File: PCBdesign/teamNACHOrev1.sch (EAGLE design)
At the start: 3 parts

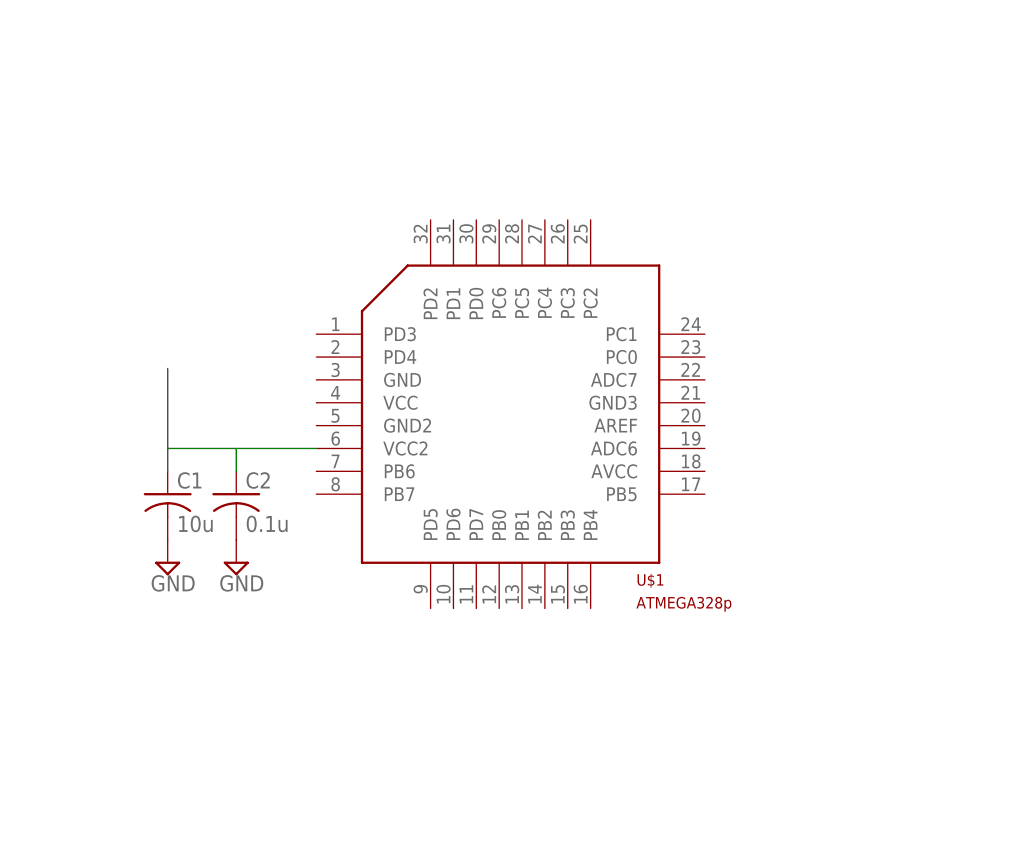
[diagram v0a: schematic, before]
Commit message: ATmega
Believe the initial set up of atmega328p has been done.
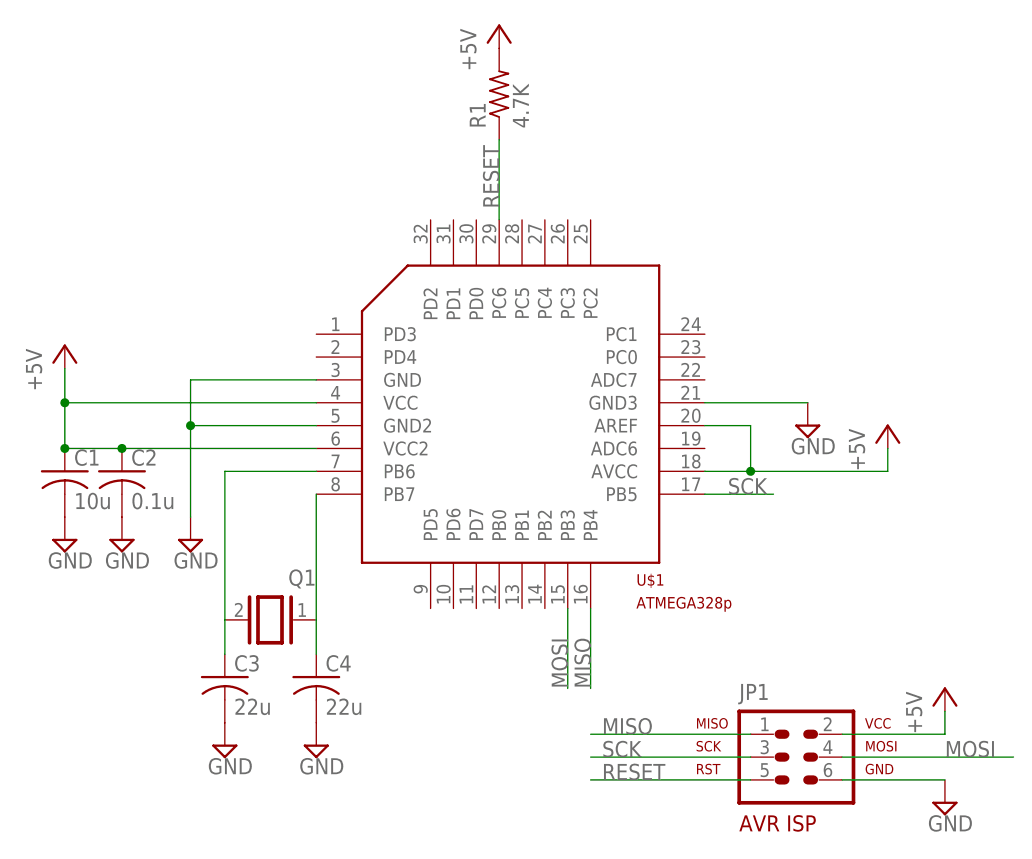
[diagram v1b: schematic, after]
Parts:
- added C3, C4: 22u, rcl:C-USC0805
- added JP1: AVR-ISP-6VERT, avr-7:AVR-ISP-6VERT
- added Q1: (no value), special:XTAL/S
- added R1: 4.7K, rcl:R-US_R0805
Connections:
- removed net N$1: C1.1, C2.1, U$1.VCC2
- new net +5V: C1.1, C2.1, JP1.2, R1.2, U$1.AREF, U$1.AVCC, U$1.VCC, U$1.VCC2
- new net MISO: JP1.1, U$1.PB4
- new net MOSI: JP1.4, U$1.PB3
- new net N$2: C3.1, Q1.2, U$1.PB6
- new net N$3: C4.1, Q1.1, U$1.PB7
- new net RESET: JP1.5, R1.1, U$1.PC6
- new net SCK: JP1.3, U$1.PB5
- net GND: now also C3.2, C4.2, JP1.6, U$1.GND, U$1.GND2, U$1.GND3
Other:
- moved on the sheet: C1, C2
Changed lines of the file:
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@@
 <layer number="48" name="Document" color="7" fill="1" visible="no" active="no"/>
 <layer number="49" name="Reference" color="7" fill="1" visible="no" active="no"/>
+<layer number="50" name="dxf" color="7" fill="1" visible="no" active="no"/>
 <layer number="51" name="tDocu" color="7" fill="1" visible="no" active="no"/>
 <layer number="52" name="bDocu" color="7" fill="1" visible="no" active="no"/>
@@
 <layer number="97" name="Info" color="7" fill="1" visible="yes" active="yes"/>
 <layer number="98" name="Guide" color="6" fill="1" visible="yes" active="yes"/>
+<layer number="200" name="200bmp" color="1" fill="10" visible="no" active="no"/>
 </layers>
 <schematic xreflabel="%F%N/%S.%C%R" xrefpart="/%S.%C%R">
@@
 <part name="SUPPLY1" library="supply2" deviceset="GND" device=""/>
 <part name="SUPPLY2" library="supply2" deviceset="GND" device=""/>
+<part name="Q1" library="special" deviceset="XTAL/S" device=""/>
+<part name="C3" library="rcl" deviceset="C-US" device="C0805" value="22u"/>
+<part name="C4" library="rcl" deviceset="C-US" device="C0805" value="22u"/>
+<part name="SUPPLY3" library="supply2" deviceset="GND" device=""/>
+<part name="SUPPLY4" library="supply2" deviceset="GND" device=""/>
+<part name="SUPPLY5" library="supply2" deviceset="GND" device=""/>
+<part name="P+1" library="supply1" deviceset="+5V" device=""/>
+<part name="SUPPLY6" library="supply2" deviceset="GND" device=""/>
+<part name="P+2" library="supply1" deviceset="+5V" device=""/>
+<part name="JP1" library="avr-7" deviceset="AVR-ISP-6" device="VERT"/>
+<part name="R1" library="rcl" deviceset="R-US_" device="R0805" value="4.7K"/>
+<part name="P+3" library="supply1" deviceset="+5V" device=""/>
+<part name="P+4" library="supply1" deviceset="+5V" device=""/>
+<part name="SUPPLY7" library="supply2" deviceset="GND" device=""/>
 </parts>
 <sheets>
@@
 <instances>
 <instance part="U$1" gate="G$1" x="86.36" y="40.64"/>
-<instance part="C1" gate="G$1" x="48.26" y="31.75"/>
-<instance part="C2" gate="G$1" x="55.88" y="31.75"/>
-<instance part="SUPPLY1" gate="GND" x="48.26" y="24.13"/>
-<instance part="SUPPLY2" gate="GND" x="55.88" y="24.13"/>
+<instance part="C1" gate="G$1" x="36.83" y="34.29"/>
+<instance part="C2" gate="G$1" x="43.18" y="34.29"/>
+<instance part="SUPPLY1" gate="GND" x="36.83" y="26.67"/>
+<instance part="SUPPLY2" gate="GND" x="43.18" y="26.67"/>
+<instance part="Q1" gate="G$1" x="59.69" y="17.78" rot="MR0"/>
+<instance part="C3" gate="G$1" x="54.61" y="11.43"/>
+<instance part="C4" gate="G$1" x="64.77" y="11.43"/>
+<instance part="SUPPLY3" gate="GND" x="54.61" y="3.81"/>
+<instance part="SUPPLY4" gate="GND" x="64.77" y="3.81"/>
+<instance part="SUPPLY5" gate="GND" x="50.8" y="26.67"/>
+<instance part="P+1" gate="1" x="36.83" y="48.26"/>
+<instance part="SUPPLY6" gate="GND" x="119.38" y="39.37"/>
+<instance part="P+2" gate="1" x="128.27" y="39.37"/>
+<instance part="JP1" gate="G$1" x="118.11" y="2.54"/>
+<instance part="R1" gate="G$1" x="85.09" y="76.2" rot="R90"/>
+<instance part="P+3" gate="1" x="85.09" y="83.82"/>
+<instance part="P+4" gate="1" x="134.62" y="10.16"/>
+<instance part="SUPPLY7" gate="GND" x="134.62" y="-2.54"/>
 </instances>
 <busses>
 </busses>
 <nets>
-<net name="N$1" class="0">
-<segment>
-<pinref part="U$1" gate="G$1" pin="VCC2"/>
-<wire x1="64.77" y1="36.83" x2="55.88" y2="36.83" width="0.1524" layer="91"/>
-<wire x1="55.88" y1="36.83" x2="48.26" y2="36.83" width="0.1524" layer="91"/>
-<wire x1="48.26" y1="36.83" x2="48.26" y2="45.72" width="0.1524" layer="91"/>
-<pinref part="C1" gate="G$1" pin="1"/>
-<wire x1="48.26" y1="36.83" x2="48.26" y2="34.29" width="0.1524" layer="91"/>
-<pinref part="C2" gate="G$1" pin="1"/>
-<wire x1="55.88" y1="36.83" x2="55.88" y2="34.29" width="0.1524" layer="91"/>
-</segment>
-</net>
 <net name="GND" class="0">
 <segment>
@@
 <pinref part="SUPPLY2" gate="GND" pin="GND"/>
 </segment>
-</net>
+<segment>
+<pinref part="C3" gate="G$1" pin="2"/>
+<pinref part="SUPPLY3" gate="GND" pin="GND"/>
+</segment>
+<segment>
+<pinref part="C4" gate="G$1" pin="2"/>
+<pinref part="SUPPLY4" gate="GND" pin="GND"/>
+</segment>
+<segment>
+<pinref part="U$1" gate="G$1" pin="GND2"/>
+<wire x1="64.77" y1="39.37" x2="50.8" y2="39.37" width="0.1524" layer="91"/>
+<wire x1="50.8" y1="39.37" x2="50.8" y2="44.45" width="0.1524" layer="91"/>
+<pinref part="U$1" gate="G$1" pin="GND"/>
+<wire x1="50.8" y1="44.45" x2="64.77" y2="44.45" width="0.1524" layer="91"/>
+<junction x="50.8" y="39.37"/>
+<wire x1="50.8" y1="39.37" x2="50.8" y2="29.21" width="0.1524" layer="91"/>
+<pinref part="SUPPLY5" gate="GND" pin="GND"/>
+</segment>
+<segment>
+<pinref part="U$1" gate="G$1" pin="GND3"/>
+<wire x1="107.95" y1="41.91" x2="119.38" y2="41.91" width="0.1524" layer="91"/>
+<pinref part="SUPPLY6" gate="GND" pin="GND"/>
+</segment>
+<segment>
+<pinref part="JP1" gate="G$1" pin="6"/>
+<wire x1="123.19" y1="0" x2="134.62" y2="0" width="0.1524" layer="91"/>
+<pinref part="SUPPLY7" gate="GND" pin="GND"/>
+</segment>
+</net>
+<net name="N$2" class="0">
+<segment>
+<pinref part="U$1" gate="G$1" pin="PB6"/>
+<pinref part="Q1" gate="G$1" pin="2"/>
+<wire x1="64.77" y1="34.29" x2="54.61" y2="34.29" width="0.1524" layer="91"/>
+<wire x1="54.61" y1="34.29" x2="54.61" y2="17.78" width="0.1524" layer="91"/>
+<wire x1="54.61" y1="17.78" x2="54.61" y2="13.97" width="0.1524" layer="91"/>
+<pinref part="C3" gate="G$1" pin="1"/>
+</segment>
+</net>
+<net name="N$3" class="0">
+<segment>
+<pinref part="U$1" gate="G$1" pin="PB7"/>
+<pinref part="Q1" gate="G$1" pin="1"/>
+<wire x1="64.77" y1="31.75" x2="64.77" y2="17.78" width="0.1524" layer="91"/>
+<wire x1="64.77" y1="17.78" x2="64.77" y2="13.97" width="0.1524" layer="91"/>
+<pinref part="C4" gate="G$1" pin="1"/>
+</segment>
+</net>
+<net name="+5V" class="0">
+<segment>
+<pinref part="U$1" gate="G$1" pin="VCC2"/>
+<wire x1="64.77" y1="36.83" x2="43.18" y2="36.83" width="0.1524" layer="91"/>
+<wire x1="43.18" y1="36.83" x2="36.83" y2="36.83" width="0.1524" layer="91"/>
+<wire x1="36.83" y1="36.83" x2="36.83" y2="41.91" width="0.1524" layer="91"/>
+<pinref part="C1" gate="G$1" pin="1"/>
+<junction x="36.83" y="36.83"/>
+<pinref part="C2" gate="G$1" pin="1"/>
+<junction x="43.18" y="36.83"/>
+<pinref part="U$1" gate="G$1" pin="VCC"/>
+<wire x1="36.83" y1="41.91" x2="36.83" y2="45.72" width="0.1524" layer="91"/>
+<wire x1="64.77" y1="41.91" x2="36.83" y2="41.91" width="0.1524" layer="91"/>
+<junction x="36.83" y="41.91"/>
+<pinref part="P+1" gate="1" pin="+5V"/>
+</segment>
+<segment>
+<pinref part="U$1" gate="G$1" pin="AVCC"/>
+<wire x1="107.95" y1="34.29" x2="113.03" y2="34.29" width="0.1524" layer="91"/>
+<wire x1="113.03" y1="34.29" x2="128.27" y2="34.29" width="0.1524" layer="91"/>
+<wire x1="128.27" y1="34.29" x2="128.27" y2="36.83" width="0.1524" layer="91"/>
+<pinref part="P+2" gate="1" pin="+5V"/>
+<pinref part="U$1" gate="G$1" pin="AREF"/>
+<wire x1="107.95" y1="39.37" x2="113.03" y2="39.37" width="0.1524" layer="91"/>
+<wire x1="113.03" y1="39.37" x2="113.03" y2="34.29" width="0.1524" layer="91"/>
+<junction x="113.03" y="34.29"/>
+</segment>
+<segment>
+<pinref part="R1" gate="G$1" pin="2"/>
+<pinref part="P+3" gate="1" pin="+5V"/>
+</segment>
+<segment>
+<pinref part="JP1" gate="G$1" pin="2"/>
+<wire x1="123.19" y1="5.08" x2="134.62" y2="5.08" width="0.1524" layer="91"/>
+<pinref part="P+4" gate="1" pin="+5V"/>
+<wire x1="134.62" y1="5.08" x2="134.62" y2="7.62" width="0.1524" layer="91"/>
+</segment>
+</net>
+<net name="SCK" class="0">
+<segment>
+<pinref part="JP1" gate="G$1" pin="3"/>
+<wire x1="113.03" y1="2.54" x2="95.25" y2="2.54" width="0.1524" layer="91"/>
+<label x="96.52" y="2.54" size="1.778" layer="95"/>
+</segment>
+<segment>
+<pinref part="U$1" gate="G$1" pin="PB5"/>
+<wire x1="107.95" y1="31.75" x2="115.57" y2="31.75" width="0.1524" layer="91"/>
+<label x="110.49" y="31.75" size="1.778" layer="95"/>
+</segment>
+</net>
+<net name="RESET" class="0">
+<segment>
+<pinref part="JP1" gate="G$1" pin="5"/>
+<wire x1="113.03" y1="0" x2="95.25" y2="0" width="0.1524" layer="91"/>
+<label x="96.52" y="0" size="1.778" layer="95"/>
+</segment>
+<segment>
+<pinref part="U$1" gate="G$1" pin="PC6"/>
+<wire x1="85.09" y1="62.23" x2="85.09" y2="71.12" width="0.1524" layer="91"/>
+<pinref part="R1" gate="G$1" pin="1"/>
+<label x="85.09" y="63.5" size="1.778" layer="95" rot="R90"/>
+</segment>
+</net>
+<net name="MISO" class="0">
+<segment>
+<pinref part="U$1" gate="G$1" pin="PB4"/>
+<wire x1="95.25" y1="19.05" x2="95.25" y2="10.16" width="0.1524" layer="91"/>
+<label x="95.25" y="10.16" size="1.778" layer="95" rot="R90"/>
+</segment>
+<segment>
+<pinref part="JP1" gate="G$1" pin="1"/>
+<wire x1="113.03" y1="5.08" x2="95.25" y2="5.08" width="0.1524" layer="91"/>
+<label x="96.52" y="5.08" size="1.778" layer="95"/>
+</segment>
+</net>
+<net name="MOSI" class="0">
+<segment>
+<pinref part="U$1" gate="G$1" pin="PB3"/>
+<wire x1="92.71" y1="19.05" x2="92.71" y2="10.16" width="0.1524" layer="91"/>
+<label x="92.71" y="10.16" size="1.778" layer="95" rot="R90"/>
+</segment>
+<segment>
+<pinref part="JP1" gate="G$1" pin="4"/>
+<wire x1="123.19" y1="2.54" x2="142.24" y2="2.54" width="0.1524" layer="91"/>
+<label x="134.62" y="2.54" size="1.778" layer="95"/>
+</segment>
+</net>

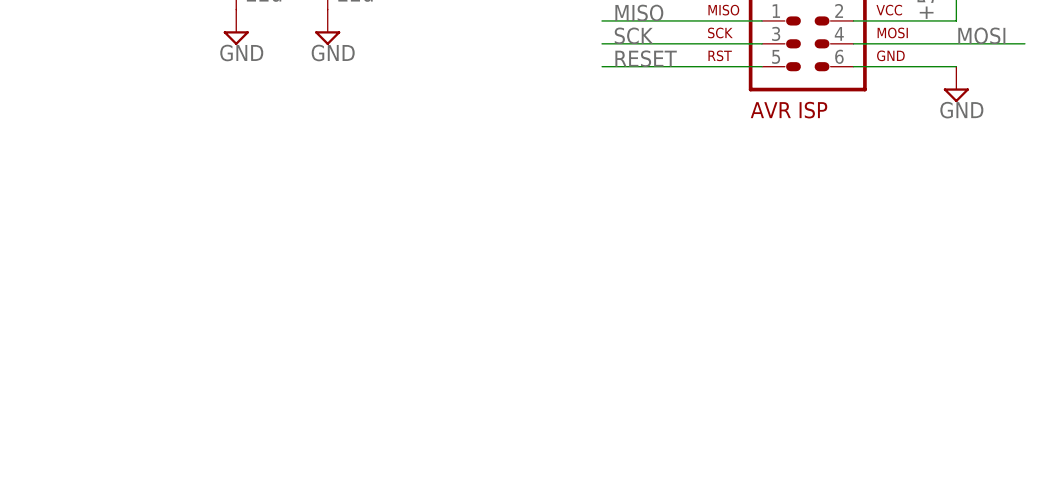
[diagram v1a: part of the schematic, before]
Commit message: Transformer Added
Created and added the transformer to circuit. Started to create flyback
circuit.
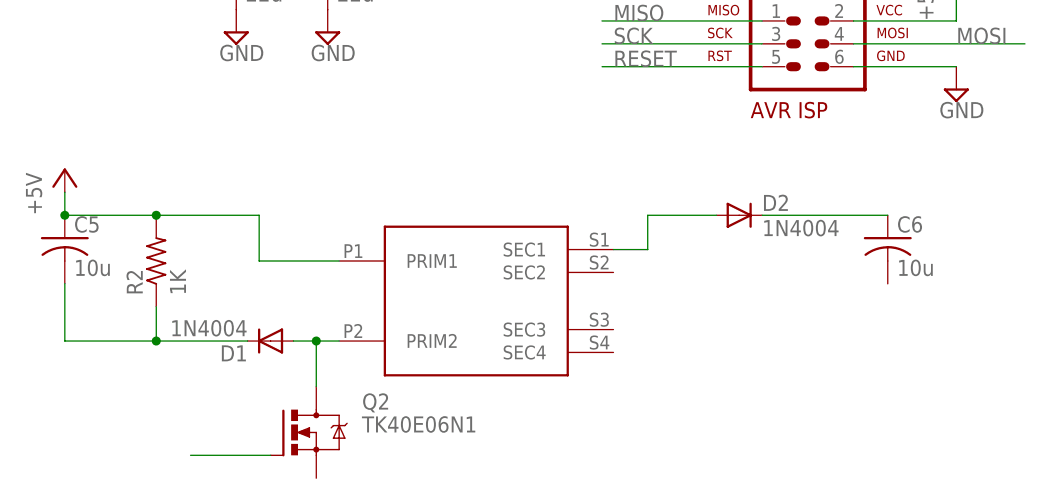
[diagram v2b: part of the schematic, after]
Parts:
- added C5, C6: 10u, rcl:C-USC0805
- added D1, D2: 1N4004, diode:1N4004
- added Q2: TK40E06N1, transistor-power:IRF520
- added R2: 1K, resistor:R-US_R0805
- added U$2: PE-63388NL, PE-63388NL:PE-63388NL
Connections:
- new net N$1: C5.2, D1.C, R2.1
- new net N$4: D1.A, Q2.D, U$2.PRIM2
- new net N$5: Q2.G
- new net N$6: D2.A, U$2.SEC1
- new net N$7: C6.1, D2.C
- net +5V: now also C5.1, R2.2, U$2.PRIM1
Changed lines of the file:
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@@
 <setting verticaltext="up"/>
 </settings>
-<grid distance="0.05" unitdist="inch" unit="inch" style="lines" multiple="1" display="no" altdistance="0.01" altunitdist="inch" altunit="inch"/>
+<grid distance="0.05" unitdist="inch" unit="inch" style="lines" multiple="1" display="yes" altdistance="0.01" altunitdist="inch" altunit="inch"/>
 <layers>
 <layer number="1" name="Top" color="4" fill="1" visible="no" active="no"/>
@@
 <layer number="97" name="Info" color="7" fill="1" visible="yes" active="yes"/>
 <layer number="98" name="Guide" color="6" fill="1" visible="yes" active="yes"/>
+<layer number="99" name="SpiceOrder" color="5" fill="1" visible="yes" active="yes"/>
 <layer number="200" name="200bmp" color="1" fill="10" visible="no" active="no"/>
 </layers>
@@
 <part name="P+4" library="supply1" deviceset="+5V" device=""/>
 <part name="SUPPLY7" library="supply2" deviceset="GND" device=""/>
+<part name="U$2" library="PE-63388NL" deviceset="PE-63388NL" device=""/>
+<part name="P+5" library="supply1" deviceset="+5V" device=""/>
+<part name="Q2" library="transistor-power" deviceset="IRF520" device="" value="TK40E06N1"/>
+<part name="D1" library="diode" deviceset="1N4004" device=""/>
+<part name="C5" library="rcl" deviceset="C-US" device="C0805" value="10u"/>
+<part name="R2" library="resistor" deviceset="R-US_" device="R0805" value="1K"/>
+<part name="D2" library="diode" deviceset="1N4004" device=""/>
+<part name="C6" library="rcl" deviceset="C-US" device="C0805" value="10u"/>
 </parts>
 <sheets>
@@
 <instance part="P+4" gate="1" x="134.62" y="10.16"/>
 <instance part="SUPPLY7" gate="GND" x="134.62" y="-2.54"/>
+<instance part="U$2" gate="G$1" x="95.25" y="-35.56"/>
+<instance part="P+5" gate="1" x="35.56" y="-11.43"/>
+<instance part="Q2" gate="G$1" x="60.96" y="-40.64"/>
+<instance part="D1" gate="1" x="58.42" y="-30.48" rot="R180"/>
+<instance part="C5" gate="G$1" x="35.56" y="-19.05"/>
+<instance part="R2" gate="G$1" x="45.72" y="-21.59" rot="R90"/>
+<instance part="D2" gate="1" x="110.49" y="-16.51"/>
+<instance part="C6" gate="G$1" x="127" y="-19.05"/>
 </instances>
 <busses>
@@
 <wire x1="134.62" y1="5.08" x2="134.62" y2="7.62" width="0.1524" layer="91"/>
 </segment>
+<segment>
+<wire x1="45.72" y1="-16.51" x2="35.56" y2="-16.51" width="0.1524" layer="91"/>
+<wire x1="35.56" y1="-16.51" x2="35.56" y2="-13.97" width="0.1524" layer="91"/>
+<pinref part="P+5" gate="1" pin="+5V"/>
+<pinref part="C5" gate="G$1" pin="1"/>
+<junction x="35.56" y="-16.51"/>
+<pinref part="R2" gate="G$1" pin="2"/>
+<wire x1="45.72" y1="-16.51" x2="57.15" y2="-16.51" width="0.1524" layer="91"/>
+<wire x1="57.15" y1="-16.51" x2="57.15" y2="-21.59" width="0.1524" layer="91"/>
+<pinref part="U$2" gate="G$1" pin="PRIM1"/>
+<wire x1="57.15" y1="-21.59" x2="66.04" y2="-21.59" width="0.1524" layer="91"/>
+<junction x="45.72" y="-16.51"/>
+</segment>
 </net>
 <net name="SCK" class="0">
@@
 </segment>
 </net>
+<net name="N$4" class="0">
+<segment>
+<pinref part="U$2" gate="G$1" pin="PRIM2"/>
+<pinref part="D1" gate="1" pin="A"/>
+<wire x1="66.04" y1="-30.48" x2="63.5" y2="-30.48" width="0.1524" layer="91"/>
+<pinref part="Q2" gate="G$1" pin="D"/>
+<wire x1="63.5" y1="-30.48" x2="60.96" y2="-30.48" width="0.1524" layer="91"/>
+<wire x1="63.5" y1="-35.56" x2="63.5" y2="-30.48" width="0.1524" layer="91"/>
+<junction x="63.5" y="-30.48"/>
+</segment>
+</net>
+<net name="N$1" class="0">
+<segment>
+<pinref part="C5" gate="G$1" pin="2"/>
+<wire x1="35.56" y1="-24.13" x2="35.56" y2="-30.48" width="0.1524" layer="91"/>
+<pinref part="D1" gate="1" pin="C"/>
+<wire x1="35.56" y1="-30.48" x2="45.72" y2="-30.48" width="0.1524" layer="91"/>
+<pinref part="R2" gate="G$1" pin="1"/>
+<wire x1="45.72" y1="-30.48" x2="55.88" y2="-30.48" width="0.1524" layer="91"/>
+<wire x1="45.72" y1="-26.67" x2="45.72" y2="-30.48" width="0.1524" layer="91"/>
+<junction x="45.72" y="-30.48"/>
+</segment>
+</net>
+<net name="N$5" class="0">
+<segment>
+<pinref part="Q2" gate="G$1" pin="G"/>
+<wire x1="58.42" y1="-43.18" x2="49.53" y2="-43.18" width="0.1524" layer="91"/>
+</segment>
+</net>
+<net name="N$6" class="0">
+<segment>
+<pinref part="U$2" gate="G$1" pin="SEC1"/>
+<wire x1="96.52" y1="-20.32" x2="100.33" y2="-20.32" width="0.1524" layer="91"/>
+<wire x1="100.33" y1="-20.32" x2="100.33" y2="-16.51" width="0.1524" layer="91"/>
+<pinref part="D2" gate="1" pin="A"/>
+<wire x1="100.33" y1="-16.51" x2="107.95" y2="-16.51" width="0.1524" layer="91"/>
+</segment>
+</net>
+<net name="N$7" class="0">
+<segment>
+<pinref part="D2" gate="1" pin="C"/>
+<pinref part="C6" gate="G$1" pin="1"/>
+<wire x1="113.03" y1="-16.51" x2="127" y2="-16.51" width="0.1524" layer="91"/>
+</segment>
+</net>
